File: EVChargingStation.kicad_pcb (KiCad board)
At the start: 2 copper layers, 173.4 x 97.2 mm, 71 parts, among them J1 Connector1, J2 Connector1, J3 FC68131, J4 FC68131, J5 FC68131, K1 G5NB-1A Relay 5VDC, Q1 PN2222A, T1 VB_05-1-12, T2 VB_05-1-12, T3 VB_05-1-12, U1 ABX00027, U2 IRM-05-5, U3 LF353P, U4 mcp6291-e_p-nd, U5 mcp6291-e_p-nd, U6 mcp6291-e_p-nd

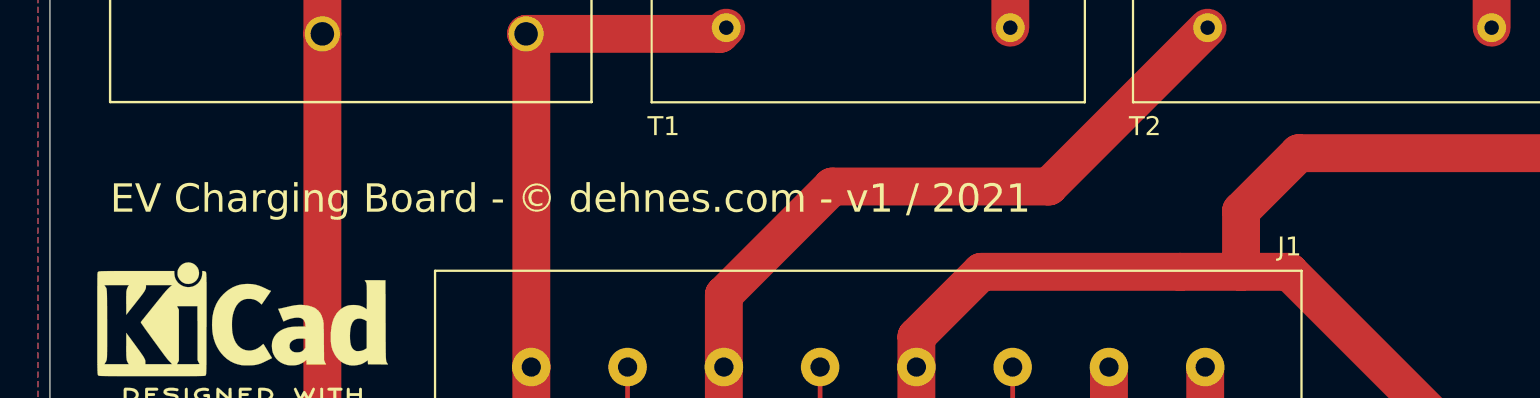
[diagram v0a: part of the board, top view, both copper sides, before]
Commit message: changed drill holes for 3.5mm minijack connector
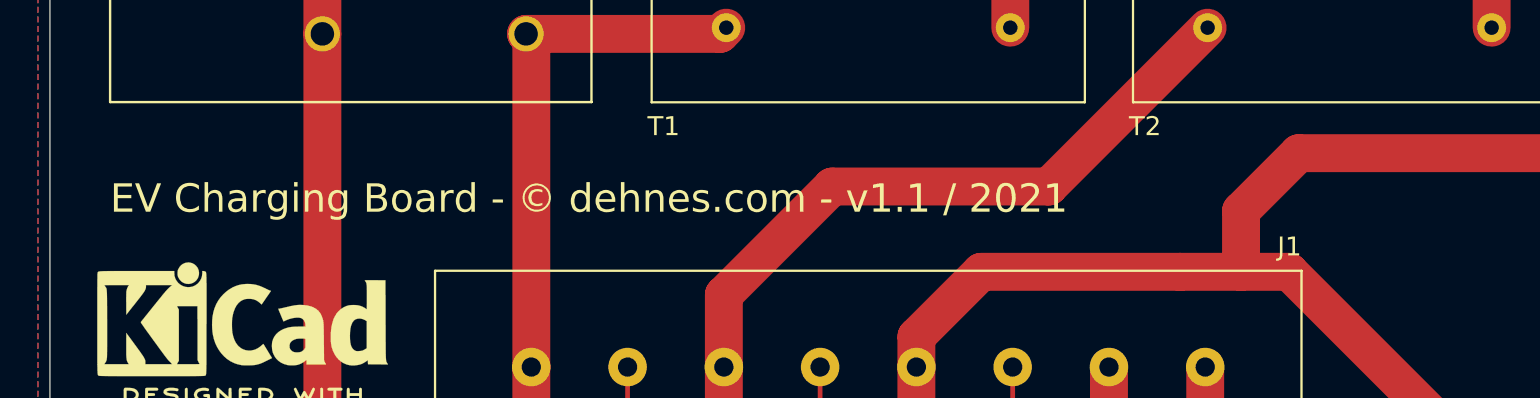
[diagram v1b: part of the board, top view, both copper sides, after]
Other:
- board text added: "EV Charging Board - © dehnes.com - v1.1 / 2021"
- board text removed: "EV Charging Board - © dehnes.com - v1 / 2021"

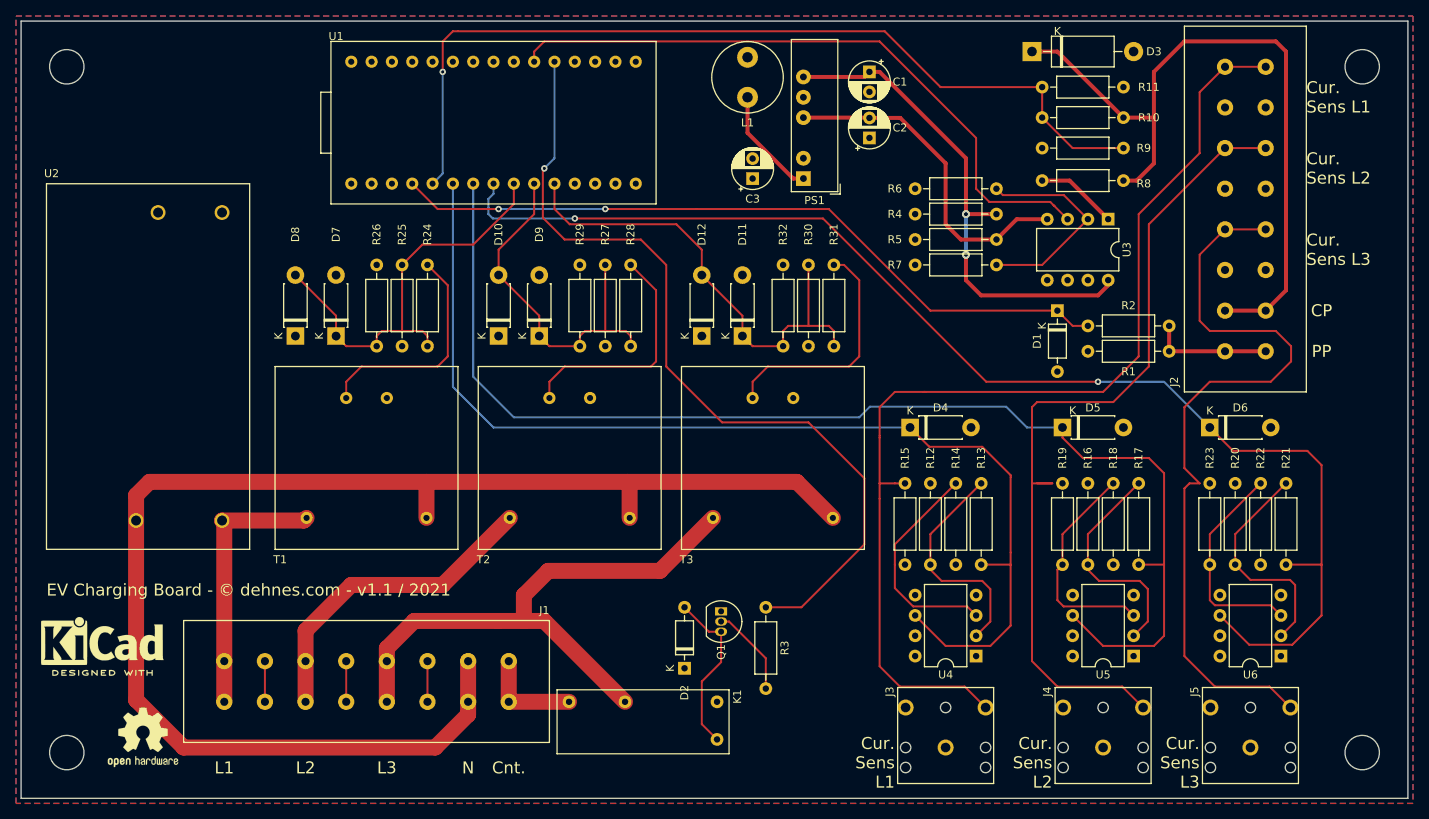
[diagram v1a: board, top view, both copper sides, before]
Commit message: revision 1.2 - added connection to PE
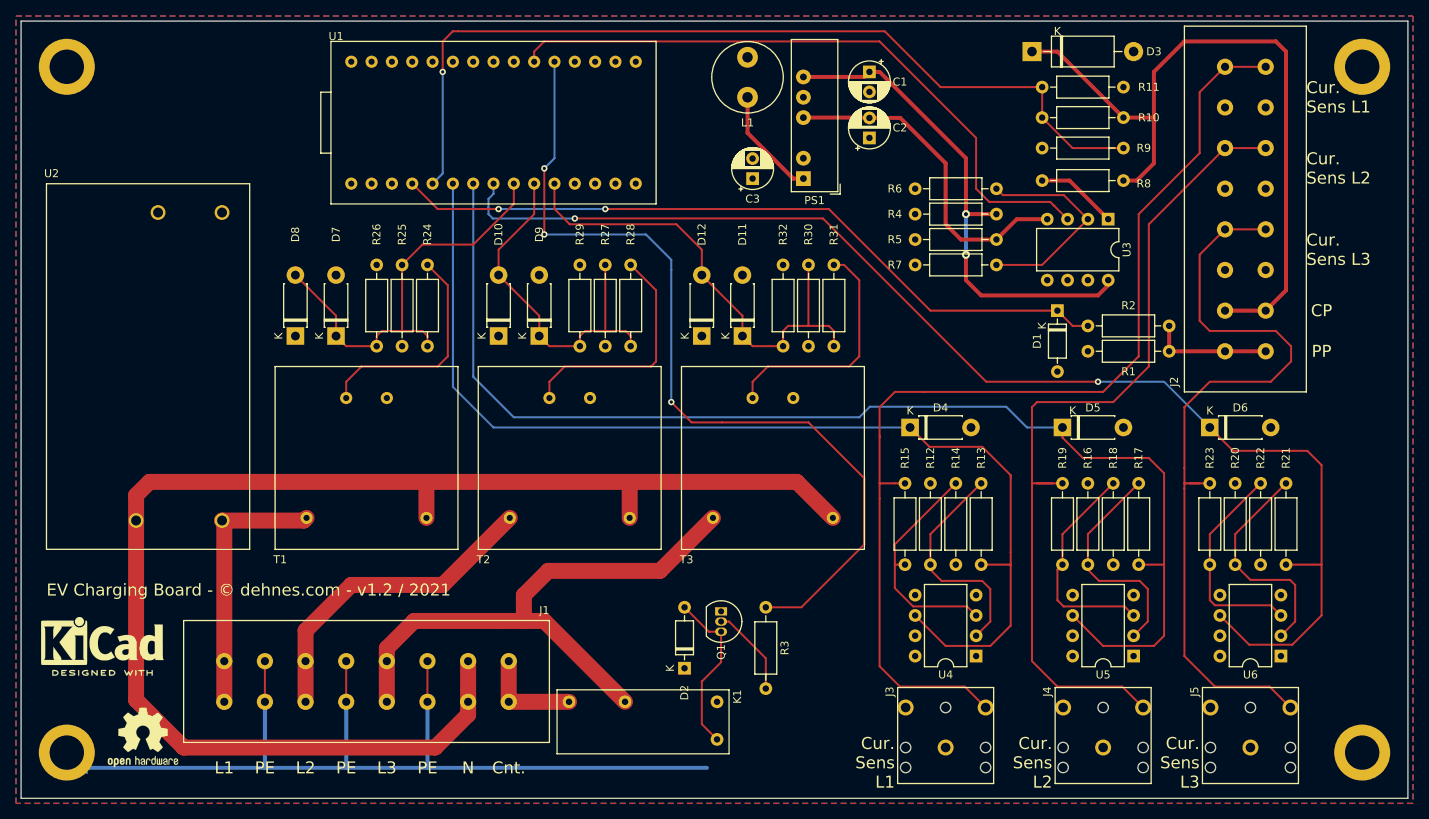
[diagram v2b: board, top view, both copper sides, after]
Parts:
- removed the REF** at (38.1, 135.9)
- removed the REF** at (200.0, 135.9)
- removed the REF** at (200.0, 50.2)
- removed the REF** at (38.1, 50.2)
- added REF**: MountingHole_4.3mm_M4_ISO14580_Pad, MountingHole:MountingHole_4.3mm_M4_ISO14580_Pad, F.Cu at (38.1, 135.9)
- added REF**: MountingHole_4.3mm_M4_ISO14580_Pad, MountingHole:MountingHole_4.3mm_M4_ISO14580_Pad, F.Cu at (200.0, 135.9)
- added REF**: MountingHole_4.3mm_M4_ISO14580_Pad, MountingHole:MountingHole_4.3mm_M4_ISO14580_Pad, F.Cu at (200.0, 50.2)
- added REF**: MountingHole_4.3mm_M4_ISO14580_Pad, MountingHole:MountingHole_4.3mm_M4_ISO14580_Pad, F.Cu at (38.1, 50.2)
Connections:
- J1 pad 2: Net-(J1-Pad2) -> GND
- J1 pad 4: Net-(J1-Pad4) -> GND
- J1 pad 6: Net-(J1-Pad6) -> GND
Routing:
- net GND: track 0.00 -> 124.4 mm
- net Net-(J1-Pad6): track 5.08 -> 0.00 mm
- net Net-(J1-Pad4): track 5.08 -> 0.00 mm
- net Net-(J1-Pad2): track 5.08 -> 0.00 mm
- net DC_RELAY: track 105.1 -> 109.3 mm, vias 1 -> 3
- net CUR_SENS_L3: track 97.5 -> 99.7 mm
- net Net-(R14-Pad1): track 27.8 -> 29.1 mm
- net CUR_SENS_L2: track 105.5 -> 106.8 mm
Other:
- board text added: "EV Charging Board - © dehnes.com - v1.2 / 2021"
- board text added: "PE"
- board text removed: "EV Charging Board - © dehnes.com - v1.1 / 2021"

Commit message: PCB layout for rev 1.3
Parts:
- removed D10, D12, D8: BZX85C4V7-TAP, Diode_THT:D_DO-41_SOD81_P7.62mm_Horizontal
- removed D11, D6, D7, D9: BZX85C3V0-TAP, Diode_THT:D_DO-41_SOD81_P7.62mm_Horizontal
- removed J2: Connector1, EVChargingStation:conn_08x02_wago
- removed R23: 10k, Resistor_THT:R_Axial_DIN0207_L6.3mm_D2.5mm_P10.16mm_Horizontal
- removed R24, R28, R31: 27k, Resistor_THT:R_Axial_DIN0207_L6.3mm_D2.5mm_P10.16mm_Horizontal
- removed R25, R27, R30: 4.7k, Resistor_THT:R_Axial_DIN0207_L6.3mm_D2.5mm_P10.16mm_Horizontal
- removed R29, R32: 8.2k, Resistor_THT:R_Axial_DIN0207_L6.3mm_D2.5mm_P10.16mm_Horizontal
- removed the REF** at (38.1, 135.9)
- removed the REF** at (200.0, 135.9)
- removed the REF** at (200.0, 50.2)
- removed the REF** at (38.1, 50.2)
- added REF**: MountingHole_6mm, EVChargingStation:MountingHole_6mm, F.Cu at (208.0, 111.0)
- added REF**: MountingHole_6mm, EVChargingStation:MountingHole_6mm, F.Cu at (168.0, 111.0)
- added REF**: MountingHole_6mm, EVChargingStation:MountingHole_6mm, F.Cu at (294.0, 191.0)
- added REF**: MountingHole_6mm, EVChargingStation:MountingHole_6mm, F.Cu at (294.0, 150.5)
- added REF**: MountingHole_6mm, EVChargingStation:MountingHole_6mm, F.Cu at (294.0, 125.5)
- added REF**: MountingHole_6mm, EVChargingStation:MountingHole_6mm, F.Cu at (122.0, 191.0)
- added REF**: MountingHole_6mm, EVChargingStation:MountingHole_6mm, F.Cu at (122.0, 151.0)
- added REF**: MountingHole_6mm, EVChargingStation:MountingHole_6mm, F.Cu at (122.0, 125.5)
- added REF**: MountingHole_6mm, EVChargingStation:MountingHole_6mm, F.Cu at (248.0, 111.0)
- D4, D5: value BZX85C3V0-TAP -> 1N4148; footprint Diode_THT:D_DO-41_SOD81_P7.62mm_Horizontal -> Diode_THT:D_DO-35_SOD27_P7.62mm_Horizontal
- R11: value 56k -> 82k
- R12, R16, R20: value 2.7k -> 10k
- R13: value 8.2k -> 10k
- R14, R18, R22: value 120k -> 10k
- R17, R21, R26: value 8.2k -> 100k
- R2: value 10k -> 1k
- R6, R7: value 100k -> 120k
- R8: value 680 -> 1k
- R9: value 100k -> 47k
- moved REF** 235.8 mm to (277.5, 142.0)
- moved REF** 212.6 mm to (260.0, 143.0)
- moved R26 158.4 mm to (223.1, 145.7), turned to 180 degrees
- moved D3 158.2 mm to (240.3, 183.8), turned to 90 degrees
- moved T1 155.7 mm to (218.0, 162.0)
- moved D2 145.9 mm to (244.1, 194.0)
- moved K1 134.9 mm to (241.0, 188.0)
- moved R8 134.9 mm to (236.5, 181.9), turned to 90 degrees
- moved R15 134.7 mm to (265.0, 159.1)
- moved Q1 131.2 mm to (245.3, 156.5)
- moved R19 129.6 mm to (279.0, 159.1)
- moved U2 128.9 mm to (143.0, 175.0)
- moved R13 122.4 mm to (254.9, 169.2), turned to 90 degrees
- moved R16 122.4 mm to (268.2, 169.2), turned to 90 degrees
- moved J1 121.3 mm to (181.0, 187.0)
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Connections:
- D1 pad 1: PP_READ -> Net-(D1-Pad1)
- D1 pad 2: GND -> Net-(D1-Pad2)
- D4 pad 1: CURRENT_SENS_L1_READ -> Net-(D4-Pad1)
- D4 pad 2: GND -> Net-(D4-Pad2)
- D5 pad 1: CURRENT_SENS_L2_READ -> Net-(D5-Pad1)
- D5 pad 2: GND -> Net-(D5-Pad2)
- J1 pad 1: MAINS_L1 -> MAINS_N
- J1 pad 2: GND -> MAINS_L3
- J1 pad 4: GND -> MAINS_L1
- J1 pad 5: MAINS_L3 -> Contactor
- J1 pad 6: GND -> Net-(J1-Pad6)
- J1 pad 7: MAINS_N -> CP
- J1 pad 8: Contactor -> /PP
- K1 pad 1: +5V -> Net-(D2-Pad2)
- K1 pad 2: MAINS_L3 -> MAINS_L1
- K1 pad 4: Net-(D2-Pad2) -> +5V
- R1 pad 1: +5V -> /PP
- R1 pad 2: PP -> +5V
- R14 pad 1: Net-(R14-Pad1) -> VOLTAGE_SENS_L1_READ
- R14 pad 2: +5V -> GND
- R15 pad 1: CUR_SENS_L1 -> GND
- R15 pad 2: Net-(R14-Pad1) -> Net-(R15-Pad2)
- R16 pad 1: GND -> Net-(R15-Pad2)
- R16 pad 2: Net-(R16-Pad2) -> CURRENT_SENS_L2_READ
- R17 pad 1: Net-(R16-Pad2) -> Net-(D4-Pad1)
- R17 pad 2: CURRENT_SENS_L2_READ -> VOLTAGE_SENS_L2_READ
- R18 pad 1: Net-(R18-Pad1) -> VOLTAGE_SENS_L2_READ
- R18 pad 2: +5V -> GND
- R19 pad 1: CUR_SENS_L2 -> GND
- R19 pad 2: Net-(R18-Pad1) -> Net-(R19-Pad2)
- R2 pad 1: PP_READ -> GND
- R2 pad 2: PP -> /PP
- R20 pad 1: GND -> Net-(R19-Pad2)
- R20 pad 2: Net-(R20-Pad2) -> CURRENT_SENS_L3_READ
- R21 pad 1: Net-(R20-Pad2) -> Net-(D5-Pad1)
- R21 pad 2: CURRENT_SENS_L3_READ -> VOLTAGE_SENS_L3_READ
- R22 pad 1: Net-(R22-Pad1) -> VOLTAGE_SENS_L3_READ
- R22 pad 2: +5V -> GND
- R26 pad 1: VOLTAGE_SENS_L1_READ -> Net-(D1-Pad1)
- R26 pad 2: +5V -> VOLTAGE_SENS_L1_READ
- R6 pad 1: Net-(R6-Pad1) -> GND
- R6 pad 2: GND -> Net-(R6-Pad2)
- R7 pad 1: +5V -> Net-(R6-Pad2)
- R7 pad 2: Net-(R6-Pad1) -> +3V3
- T1 pad 3: Net-(R24-Pad2) -> Net-(D1-Pad2)
- T2 pad 3: Net-(R28-Pad2) -> Net-(D4-Pad2)
- T3 pad 3: Net-(R31-Pad2) -> Net-(D5-Pad2)
- U1 pad 2: Net-(U1-Pad2) -> +3V3
- U1 pad 4: PP_READ -> /PP
- U3 pad 2: Net-(R6-Pad1) -> Net-(R6-Pad2)
- U3 pad 5: (no net) -> GND
- U3 pad 6: (no net) -> Net-(U3-Pad6)
- U3 pad 7: (no net) -> Net-(U3-Pad6)
- U4 pad 3: Net-(R14-Pad1) -> CUR_SENS_L1
- U4 pad 4: +5V -> +3V3
- U5 pad 2: Net-(R16-Pad2) -> Net-(R15-Pad2)
- U5 pad 3: Net-(R18-Pad1) -> CUR_SENS_L2
- U5 pad 4: +5V -> +3V3
- U6 pad 2: Net-(R20-Pad2) -> Net-(R19-Pad2)
- U6 pad 3: Net-(R22-Pad1) -> CUR_SENS_L3
- U6 pad 4: +5V -> +3V3
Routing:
- net +5V: track 0.00 -> 261.9 mm, vias 0 -> 2
- net /PP: track 0.00 -> 176.7 mm, vias 0 -> 4
- net +3V3: track 0.00 -> 168.4 mm, vias 0 -> 4
- net GND: track 124.4 -> 0.00 mm
- net CUR_SENS_L1: track 132.6 -> 11.8 mm
- net CUR_SENS_L2: track 106.8 -> 12.0 mm
- net PP_READ: track 91.8 -> 0.00 mm, vias 2 -> 0
- net CP: track 91.9 -> 181.3 mm, vias 0 -> 2
- net CUR_SENS_L3: track 99.7 -> 11.5 mm
- net CP_READ: track 112.2 -> 30.6 mm, vias 1 -> 0
- net MAINS_L1: track 33.5 -> 105.2 mm
- net MAINS_L3: track 72.9 -> 22.4 mm
- net CURRENT_SENS_L3_READ: track 159.5 -> 204.0 mm, vias 2 -> 0
- net Net-(R8-Pad2): track 10.3 -> 54.3 mm, vias 0 -> 2
- net Contactor: track 12.6 -> 50.2 mm
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- removed copper zone on F.Cu, net +5V
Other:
- board size 173.4 x 97.2 mm -> 188 x 98 mm
- net class Default: clearance 0.2 -> 0.4; trace_width 0.25 -> 0.6
- net class POWER removed
- rule trace_clearance: 0.2 -> 0.4
- board text added: "C.sens.L1"
- board text added: "C.sens.L2"
- board text added: "C.sens.L3"
- board text added: "DehneEVSE"
- board text added: "dehnes.com - rev 1.3"
- board text removed: "Cur. Sens L1"
- board text removed: "Cur. Sens L2"
- board text removed: "Cur. Sens L3"
- board text removed: "EV Charging Board - © dehnes.com - v1.2 / 2021"
- board text removed: "PE"

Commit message: revision 1.3 done
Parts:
- removed the R10 at (182.5, 118.4)
- removed the R11 at (182.5, 121.6)
- removed the R4 at (237.1, 121.0)
- removed the R5 at (233.9, 121.0)
- added D6: 1N4148, Diode_THT:D_DO-35_SOD27_P7.62mm_Horizontal, F.Cu at (191.2, 118.8)
- added R7: 180k, Resistor_THT:R_Axial_DIN0207_L6.3mm_D2.5mm_P10.16mm_Horizontal, F.Cu at (182.5, 121.7)
- PS1: value IA0512S -> NMA0512SC
- U1: value ABX00027 -> Arduino Nano 33 IoT
- U3: value LF353P -> LT1498IN8#PBF
- moved R4 6.18 mm to (243.2, 132.8)
- moved R5 6.18 mm to (233.0, 136.0)
- moved U3 6.18 mm to (234.3, 120.7)
- renumbered R26 to R10, R18 to R11, R17 to R12, R22 to R13, R21 to R14, R12 to R15, R13 to R16, R15 to R17, R16 to R18, R6 to R4, R7 to R5, R8 to R6, R9 to R8, R14 to R9
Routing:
- net +5V: track 261.9 -> 249.5 mm
- net PWM: track 111.6 -> 103.4 mm
- net -12VDC: track 22.8 -> 16.4 mm
- net +12VDC: track 30.0 -> 24.2 mm
- net Net-(D6-Pad1): track 0.00 -> 3.49 mm
- net CP_READ: track 30.6 -> 28.0 mm
- net CP: track 181.3 -> 178.8 mm
- net Net-(R6-Pad2): track 54.3 -> 52.8 mm
- net +3V3: track 168.4 -> 169.4 mm, vias 4 -> 0
- net VOLTAGE_SENS_L3_READ: vias 2 -> 1
- net DC_RELAY: vias 1 -> 0
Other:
- net class Default: clearance 0.4 -> 0.2
- rule trace_clearance: 0.4 -> 0.2
